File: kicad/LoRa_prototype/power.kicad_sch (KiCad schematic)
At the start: 56 parts, among them J15 SYS, J2 USB_C_Receptacle_PowerOnly_6P, J3 BAT, J5 FG, J6 FG, J7 BQ, U2 BQ24074RGTT

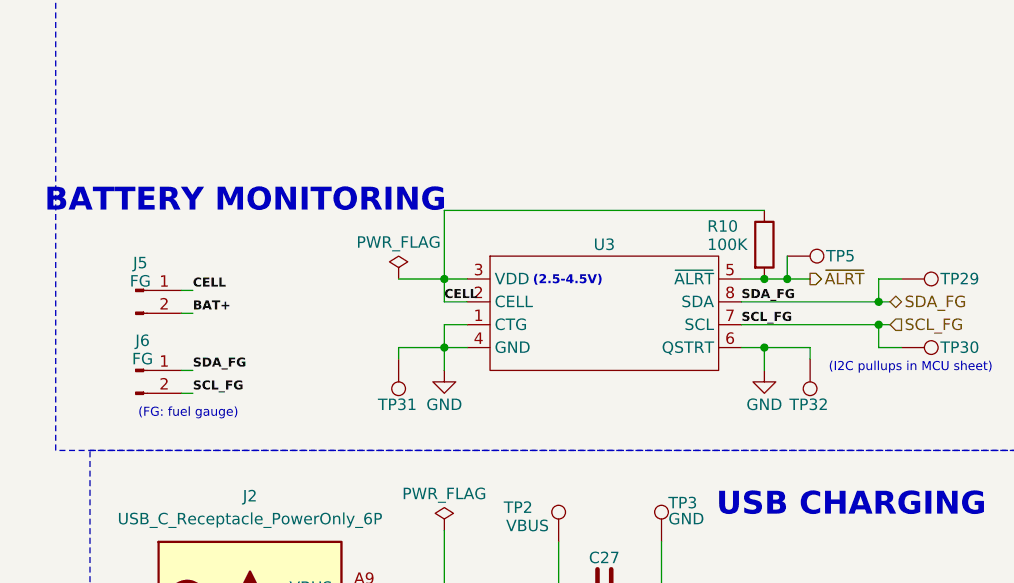
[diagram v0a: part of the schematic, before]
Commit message: Removed redundant I2C test pin headers
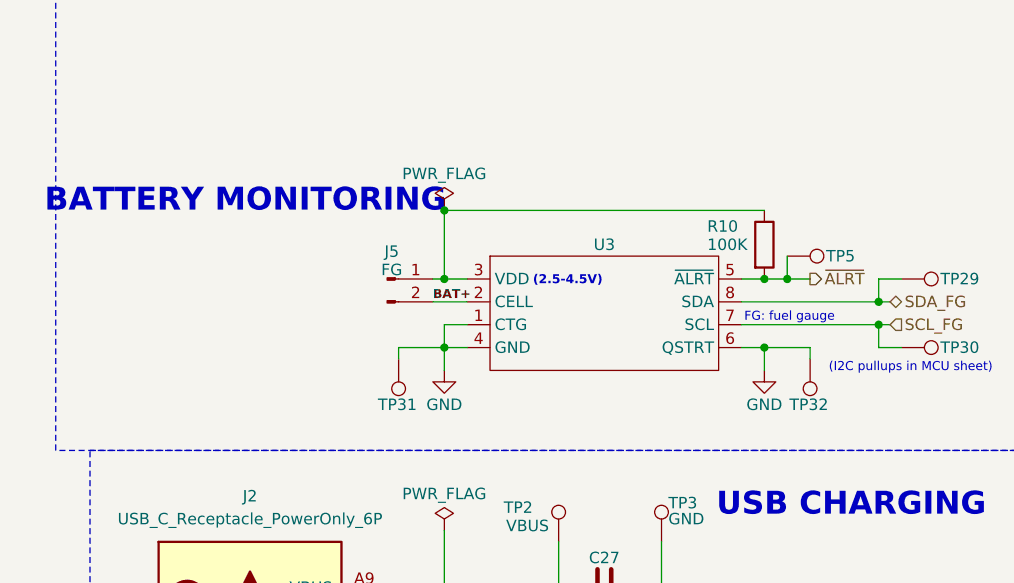
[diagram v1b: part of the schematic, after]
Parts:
- removed J6: FG, Connector_PinHeader_2.54mm:PinHeader_1x02_P2.54mm_Vertical, symbol Connector:Conn_01x02_Pin
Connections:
- net BAT+: now also U3.2 (CELL)
- net CELL: no longer names the net of J5.1 (Pin_1), R10.1, U3.3 (VDD)
- net CELL: no longer U3.2 (CELL)
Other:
- note added: "FG: fuel gauge"
- note removed: "(FG: fuel gauge)"
- moved on the sheet: J5

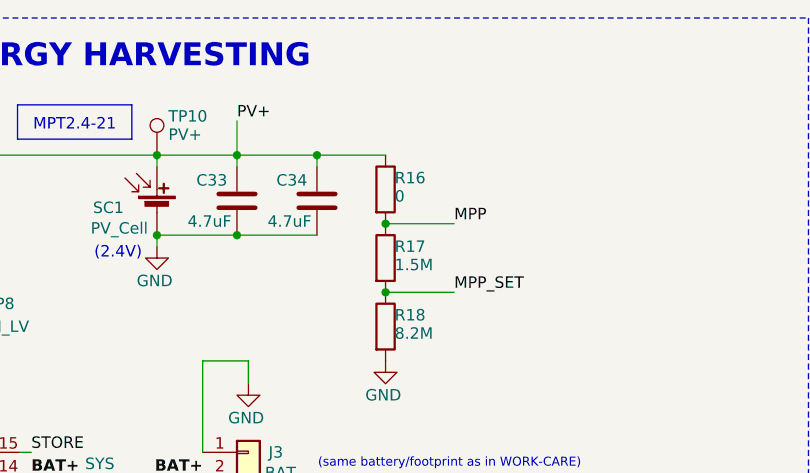
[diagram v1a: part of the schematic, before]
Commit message: Updated component values to match E24 series
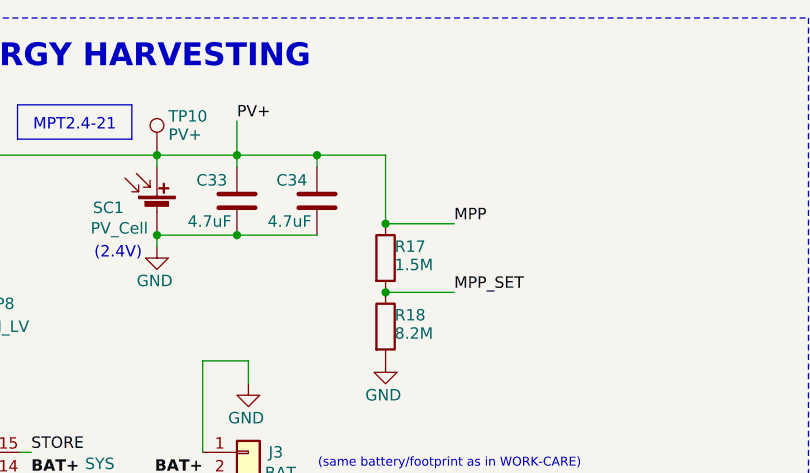
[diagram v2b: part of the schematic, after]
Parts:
- removed R16: 0, Resistor_SMD:R_0805_2012Metric, symbol Device:R
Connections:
- net PV+ is gone; now on net MPP: C33.2, C34.2, L7.2, SC1.1 (+), TP10.1, U4.13 (CONF)

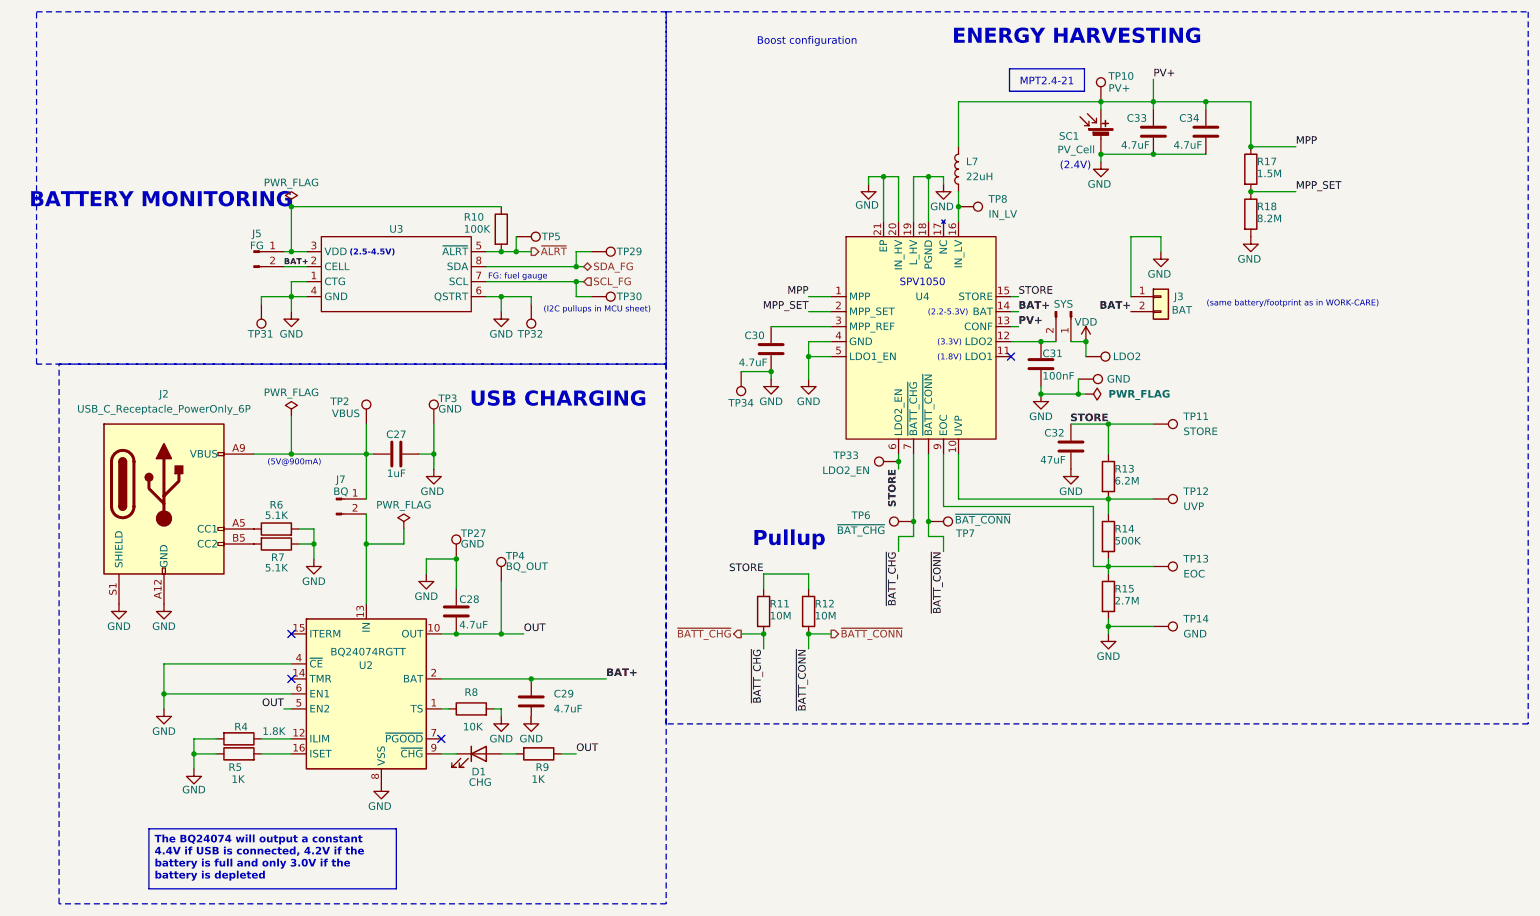
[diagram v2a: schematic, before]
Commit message: Added 3.3V 500mA LDO
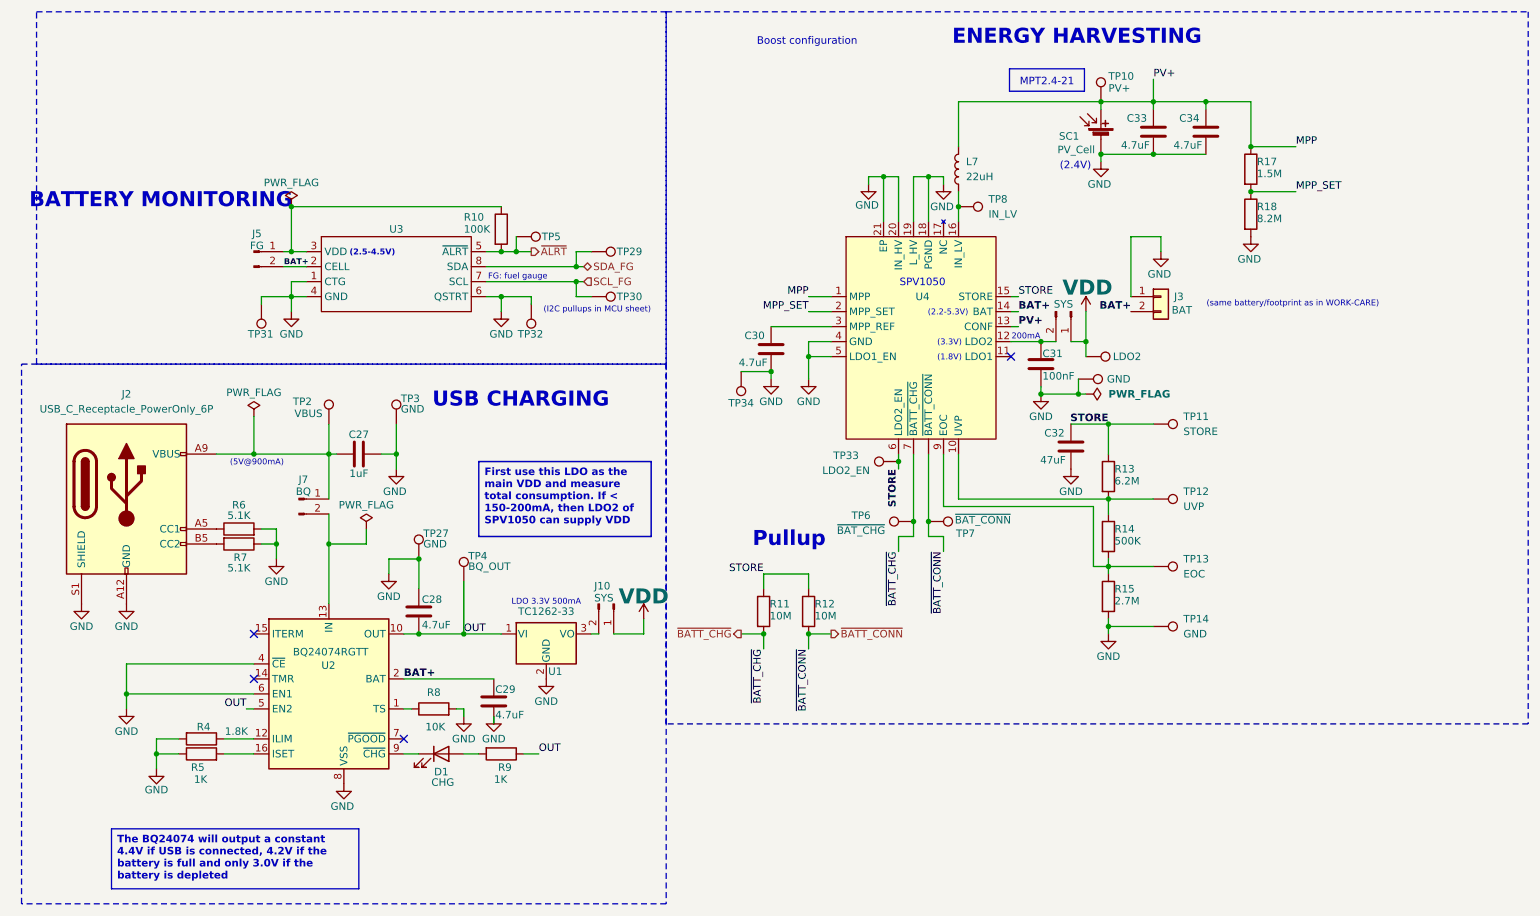
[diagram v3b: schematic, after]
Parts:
- added J10: SYS, Connector_PinHeader_2.54mm:PinHeader_1x02_P2.54mm_Vertical, symbol Connector:Conn_01x02_Pin
- added U1: TC1262-33, symbol Regulator_Linear:TC1262-33
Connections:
- net GND: now also U1.2 (GND)
- net OUT: now also U1.1 (VI)
- net VDD: now also J10.1 (Pin_1)
- new net: J10.2 (Pin_2), U1.3 (VO)
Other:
- note added: "200mA"
- note added: "LDO 3.3V 500mA"
- moved on the sheet: C27, C28, C29, D1, J2, J7, R4, R5, R6, R7, R8, R9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

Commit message: Assigned most footprints
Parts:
- L7: footprint (none) -> Inductor_SMD:L_0402_1005Metric
- U1: footprint (none) -> footprints:SOT-223-3
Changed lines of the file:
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@@
 			)
 		)
-		(property "Footprint" ""
+		(property "Footprint" "footprints:SOT-223-3"
 			(at 116.84 117.475 0)
 			(hide yes)
@@
 			)
 		)
-		(property "Footprint" ""
+		(property "Footprint" "Inductor_SMD:L_0402_1005Metric"
 			(at 186.69 44.45 0)
 			(hide yes)

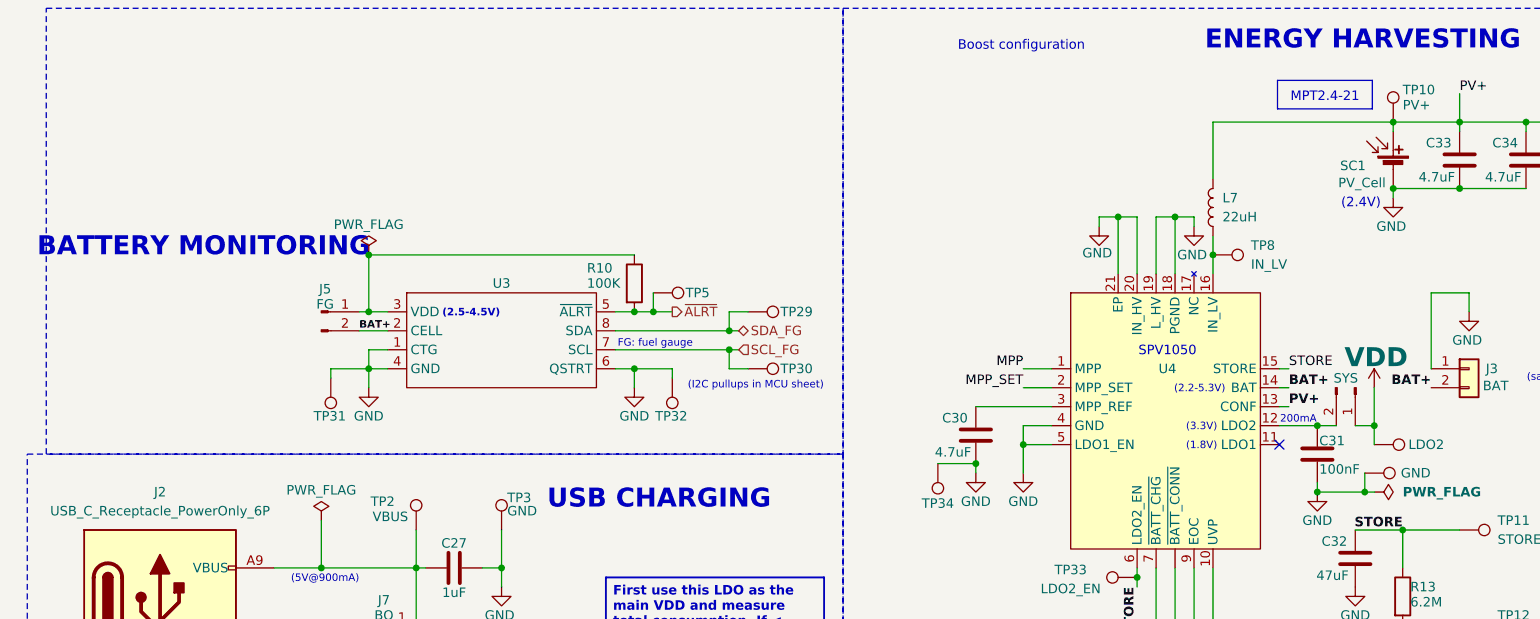
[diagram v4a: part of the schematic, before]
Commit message: Assigned almost all footprints
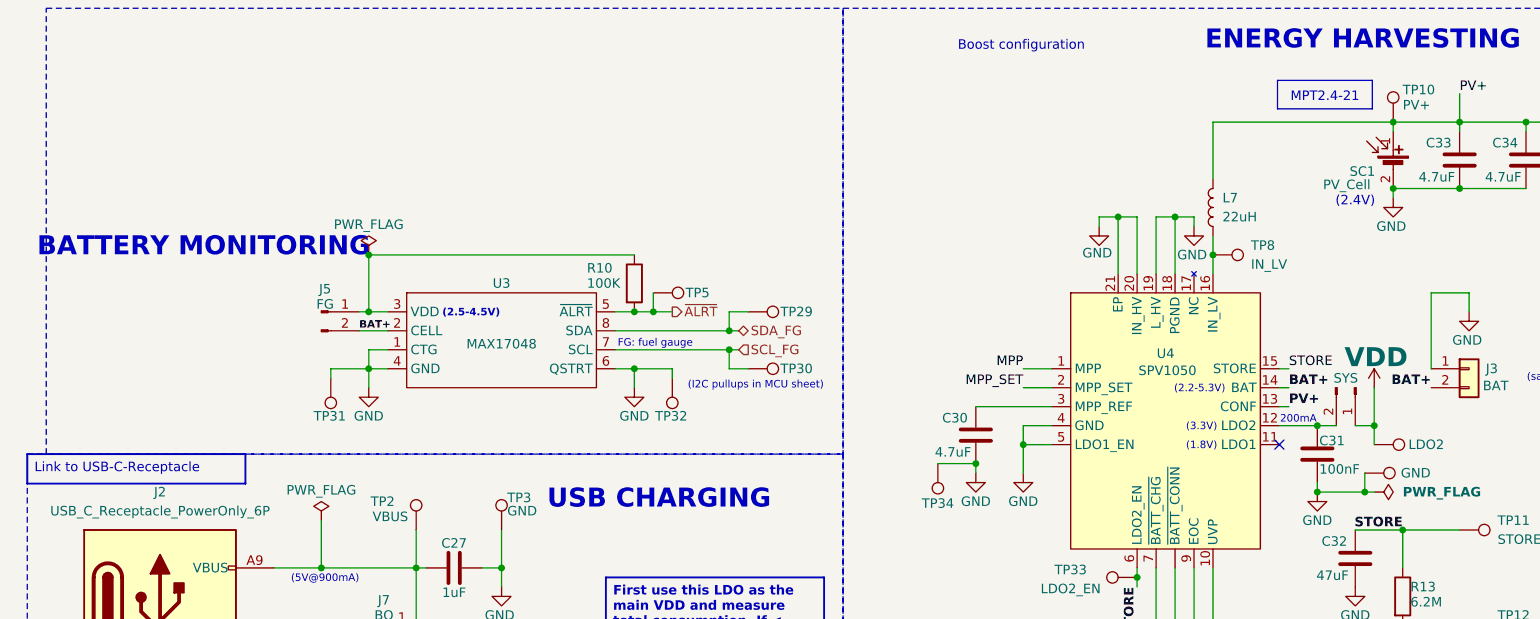
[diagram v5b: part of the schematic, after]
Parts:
- J2: footprint (none) -> footprints:UC17-0B06F68011
- SC1: footprint (none) -> footprints:MPT2.4-21
- U3: value (none) -> MAX17048; footprint (none) -> footprints:SON50P200X200X80-9N
- U4: value (none) -> SPV1050; footprint (none) -> footprints:QFN40P300X300X100-21N
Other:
- note removed: "SPV1050"

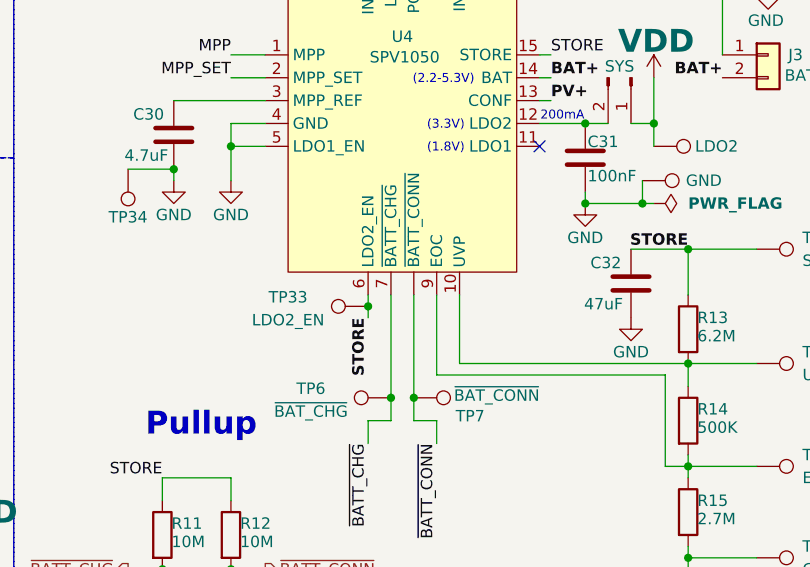
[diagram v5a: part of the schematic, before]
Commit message: Started PCB Layout (Milestone)
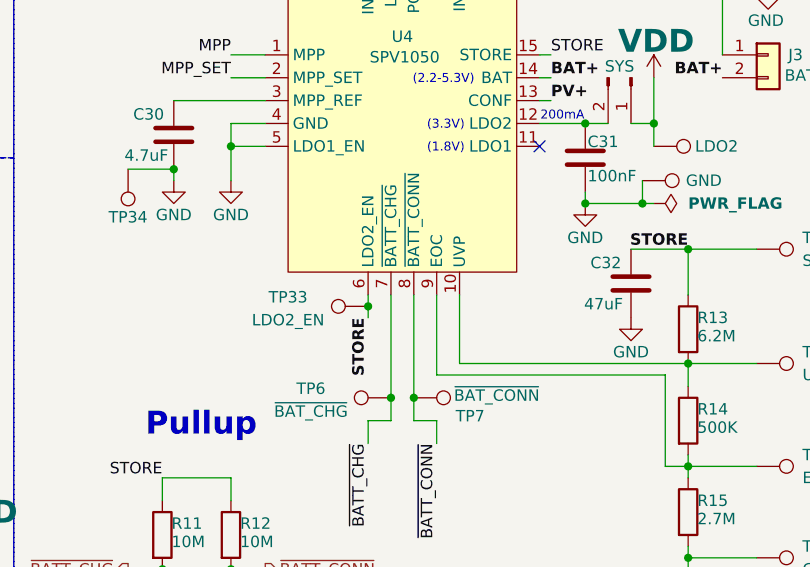
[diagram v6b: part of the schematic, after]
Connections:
- net ~{BATT_CONN}: now also U4.8 (~{BATT_CONN}); no longer U4. (~{BATT_CONN})
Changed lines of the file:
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@@
 		(pin "5"
 		)
-		(pin ""
+		(pin "8"
 		)
 		(pin "17"
